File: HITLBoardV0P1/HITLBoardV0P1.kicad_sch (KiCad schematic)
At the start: 0 parts

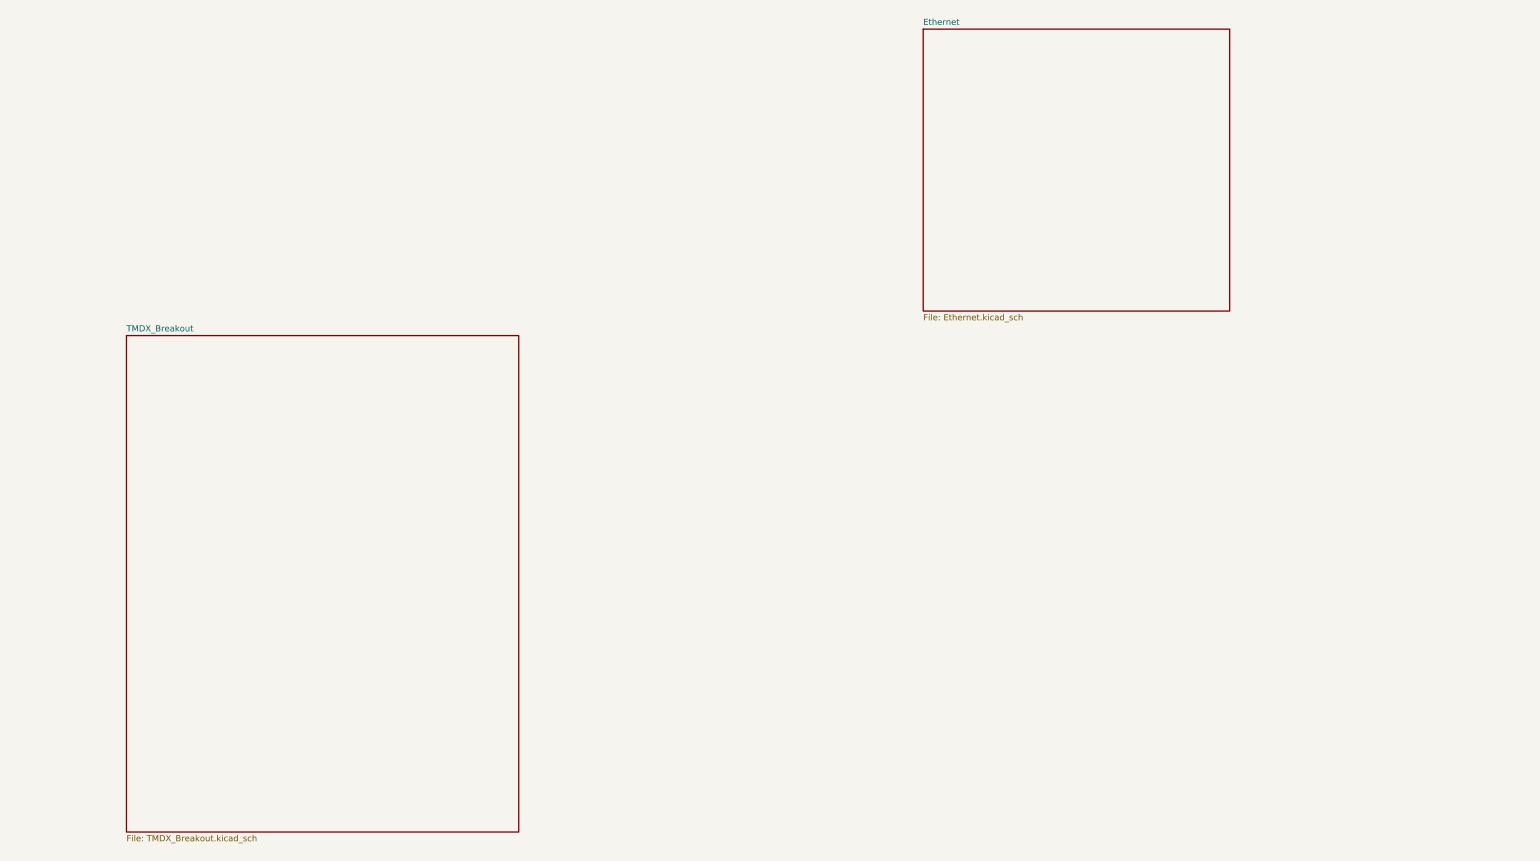
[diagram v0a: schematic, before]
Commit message: complete ethernet schematic capture
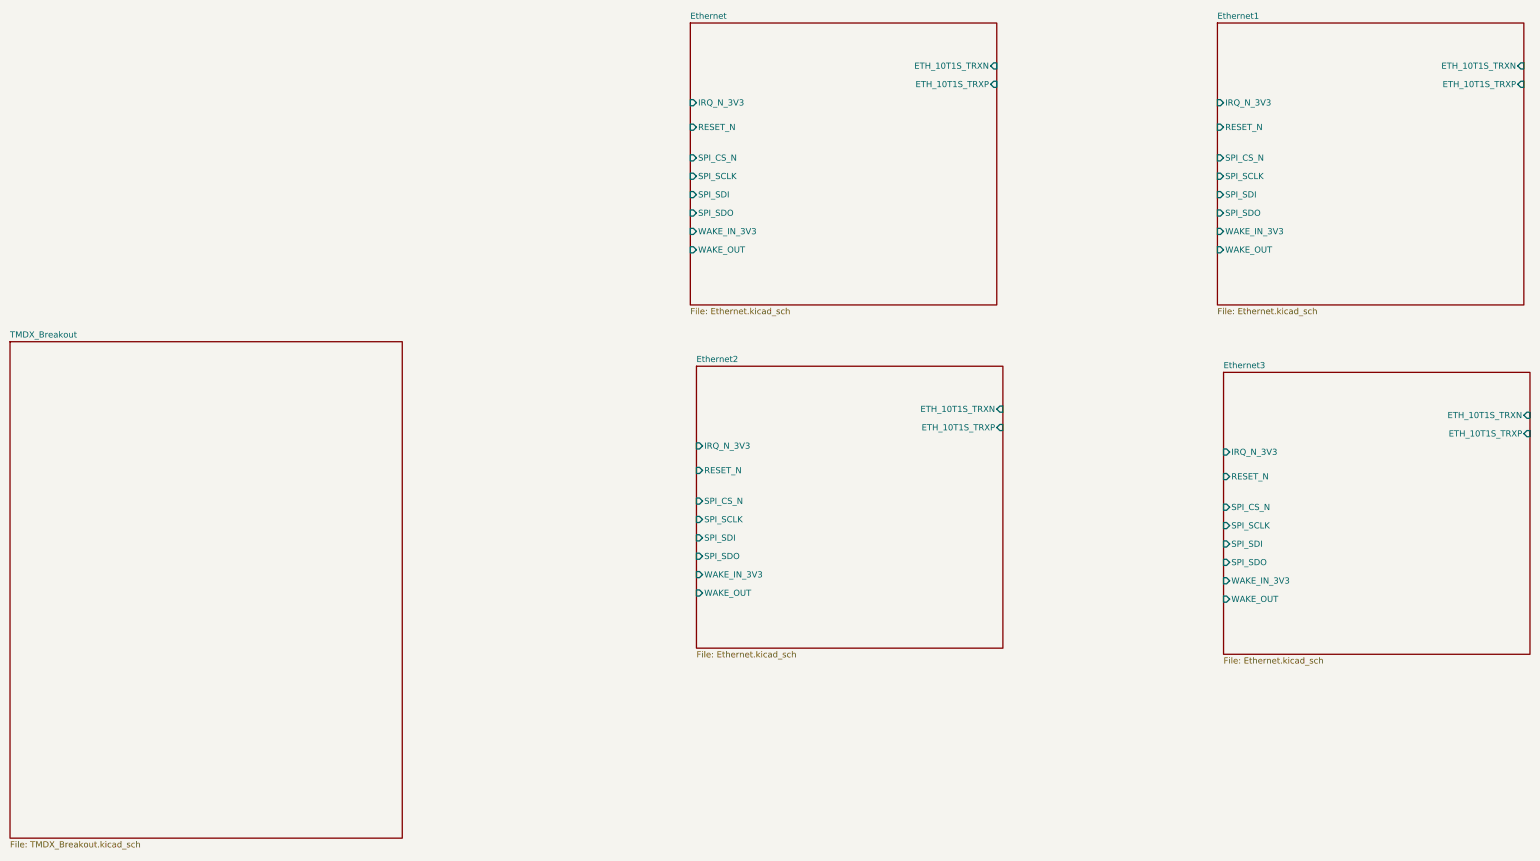
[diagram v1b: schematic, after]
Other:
- added sheet Ethernet1 (Ethernet.kicad_sch)
- added sheet Ethernet2 (Ethernet.kicad_sch)
- added sheet Ethernet3 (Ethernet.kicad_sch)
- sheet Ethernet ports: added ETH_10T1S_TRXN, ETH_10T1S_TRXP, IRQ_N_3V3, RESET_N, SPI_CS_N, SPI_SCLK, SPI_SDI, SPI_SDO, WAKE_IN_3V3, WAKE_OUT; removed none

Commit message: UPDATE -- IN PROGRESS
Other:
- removed sheet Ethernet1
- removed sheet Ethernet3
- added sheet RaspberryPiPico (RaspberryPiPico.kicad_sch)
- sheet Ethernet ports: added ETH_10T1S_TRXN_N, ETH_10T1S_TRXP_P; removed ETH_10T1S_TRXN, ETH_10T1S_TRXP
- sheet Ethernet2: file Ethernet.kicad_sch -> Ethernet2.kicad_sch

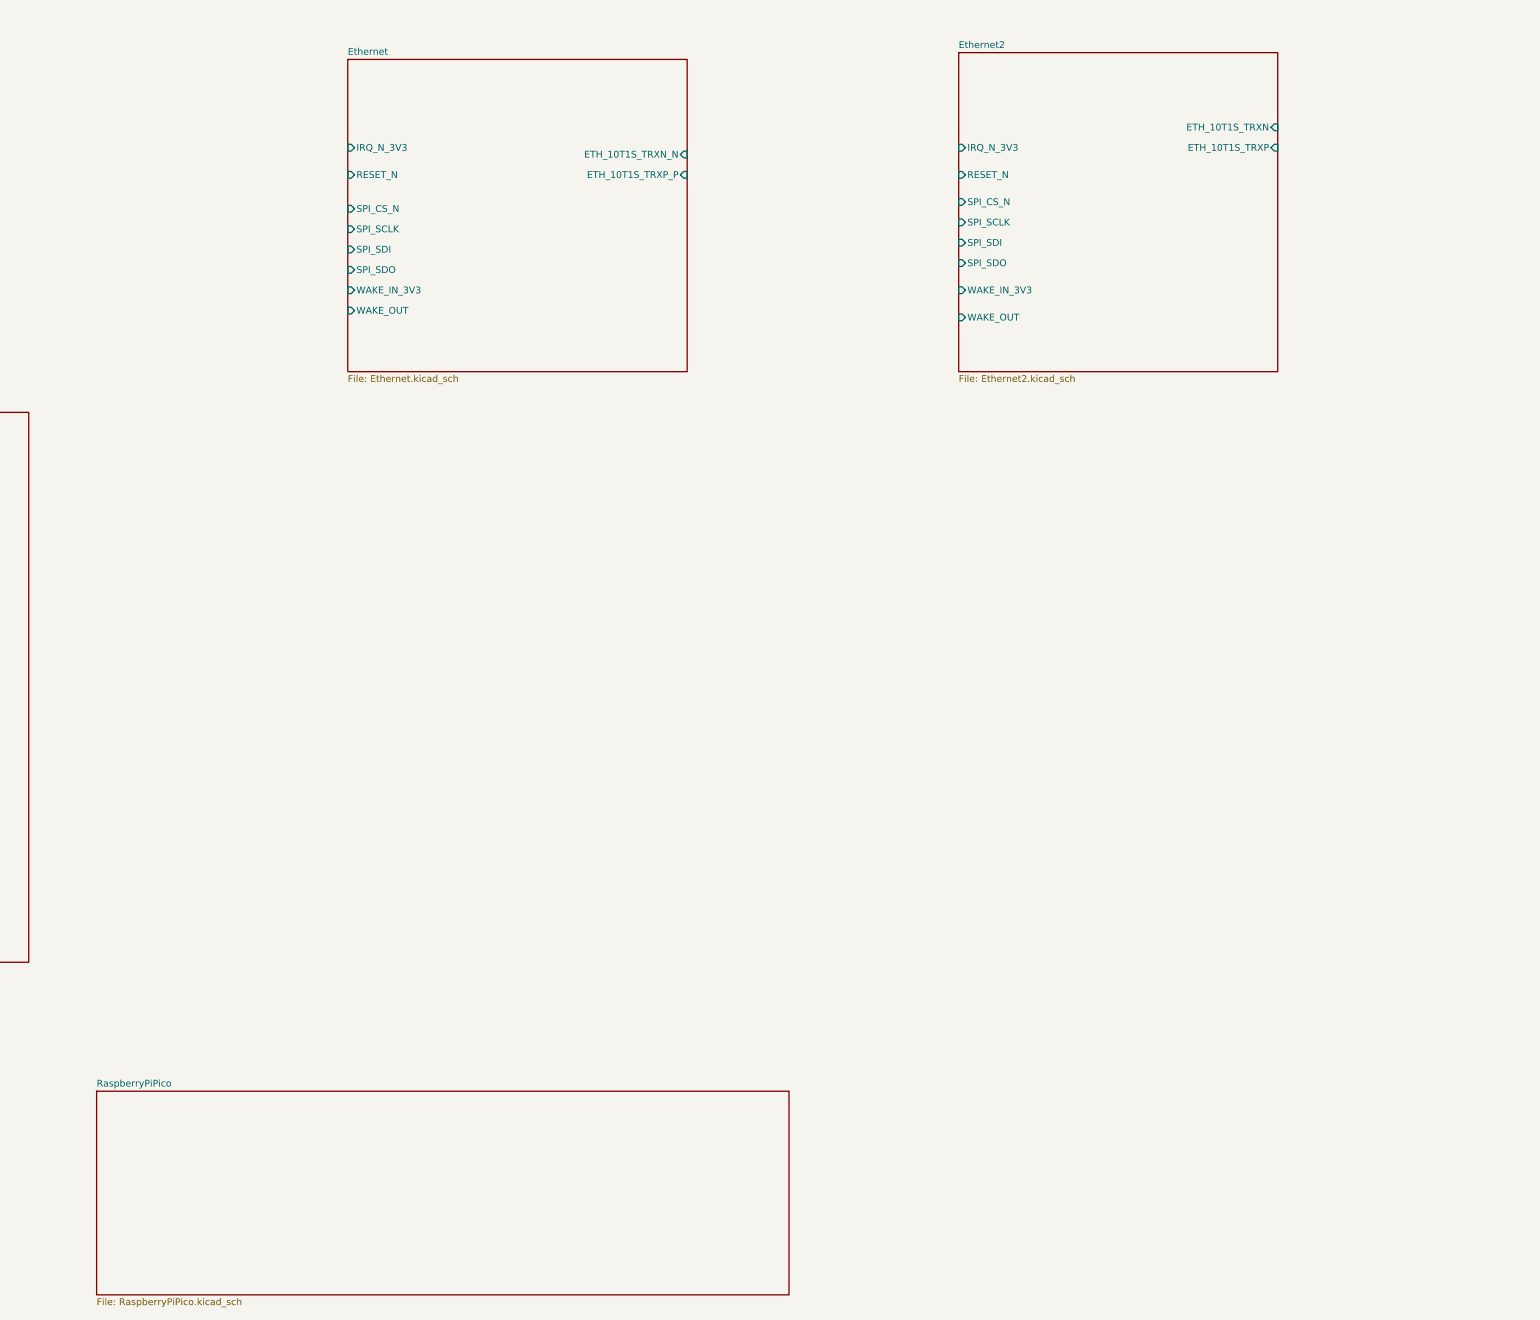
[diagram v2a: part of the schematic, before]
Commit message: in progress, brute forced lan8650 layouts :( damn you kicad
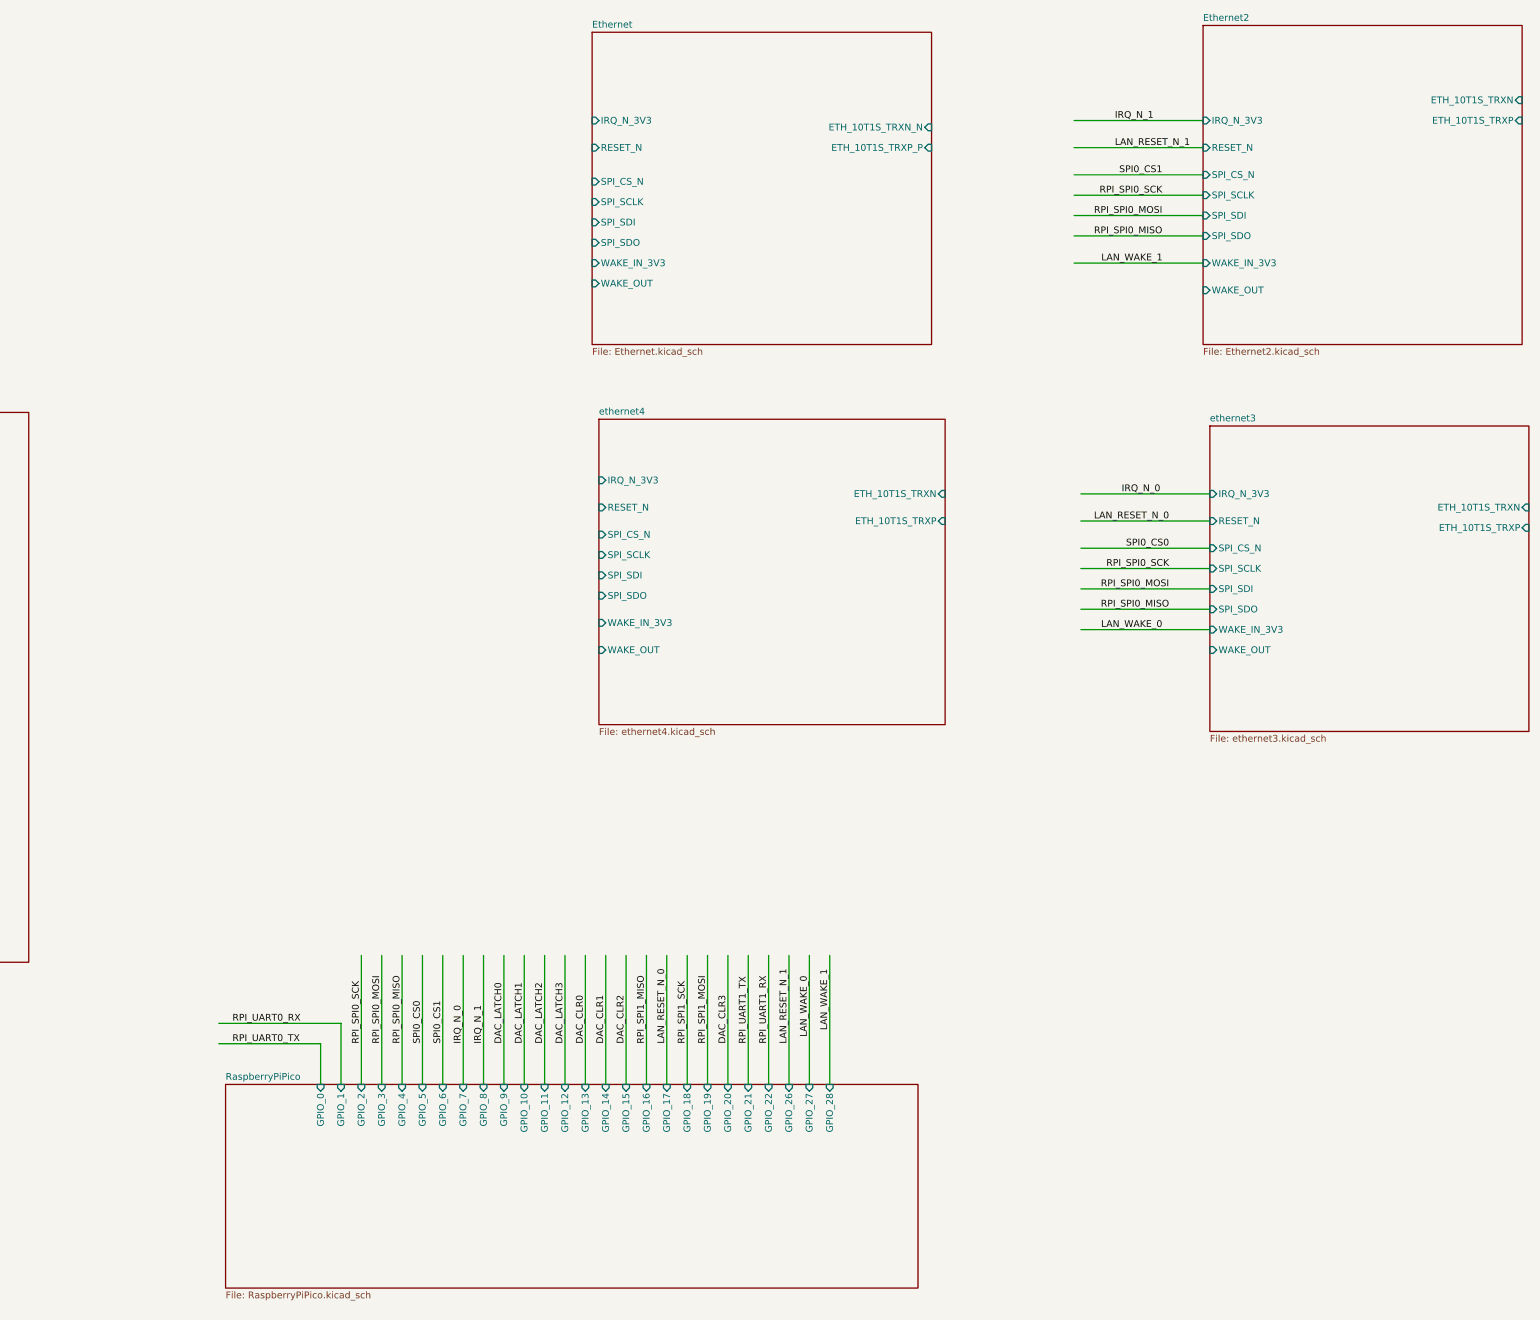
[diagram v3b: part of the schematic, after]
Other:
- added sheet ethernet3 (ethernet3.kicad_sch)
- added sheet ethernet4 (ethernet4.kicad_sch)
- sheet RaspberryPiPico ports: added GPIO_0, GPIO_1, GPIO_10, GPIO_11, GPIO_12, GPIO_13, GPIO_14, GPIO_15, GPIO_16, GPIO_17, GPIO_18, GPIO_19, GPIO_2, GPIO_20, GPIO_21, GPIO_22, GPIO_26, GPIO_27, GPIO_28, GPIO_3, GPIO_4, GPIO_5, GPIO_6, GPIO_7, GPIO_8, GPIO_9; removed none

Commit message: update
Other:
- added sheet DAC (DAC.kicad_sch)

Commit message: UPDATE IN PROGRESS, 4 DACS ADDED AND INITIAL ROUTED IN PCB
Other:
- added sheet dac2 (dac2.kicad_sch)
- added sheet dac3 (DAC3.kicad_sch)
- added sheet dac4 (dac4.kicad_sch)
- sheet DAC ports: added CLR, CURRENT_OUT, DIN, LATCH, SCLK, SDO; removed none
